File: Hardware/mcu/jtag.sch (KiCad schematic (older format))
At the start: 1 part, among them P301 ARM_JTAG_10PIN

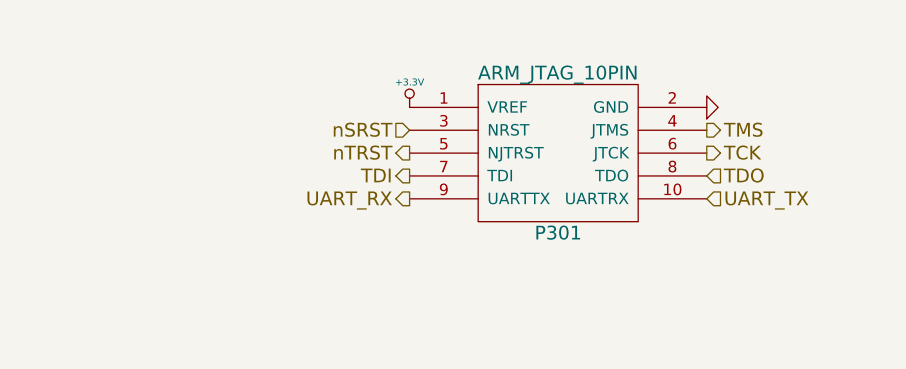
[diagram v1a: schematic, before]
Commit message: changes to mcu, new format and using a display adapter board
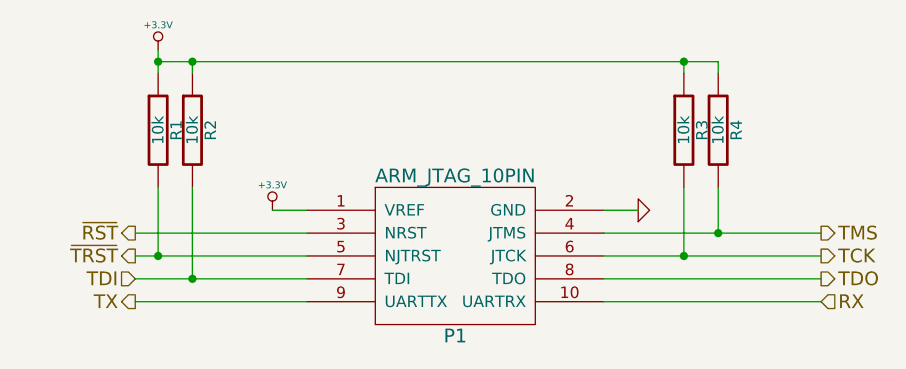
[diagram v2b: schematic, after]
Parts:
- removed P301: ARM_JTAG_10PIN, symbol ARM_JTAG_10PIN
- added P1: ARM_JTAG_10PIN, symbol ARM_JTAG_10PIN
- added R1, R2, R3, R4: 10k, symbol R
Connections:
- net +3.3V: now also P1.1 (VREF), R1.1, R2.1, R3.1, R4.1
- net GND: now also P1.2 (GND)
- net TCK: now also P1.6 (JTCK), R3.2
- net TDI: now also P1.7 (TDI), R2.2
- net TDO: now also P1.8 (TDO)
- net TMS: now also P1.4 (JTMS), R4.2
- new net RX: P1.10 (UARTRX)
- new net TX: P1.9 (UARTTX)
- new net ~RST: P1.3 (NRST)
- new net ~TRST: P1.5 (NJTRST), R1.2
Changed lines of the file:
@@
-EESchema Schematic File Version 2  date Di 17 Mai 2011 02:16:23 CEST
+EESchema Schematic File Version 2  date So 17 Jul 2011 02:24:16 CEST
 LIBS:power
 LIBS:device
@@
 LIBS:valves
 LIBS:nhesse
-LIBS:bordcomputer-cache
+LIBS:mcu-cache
 EELAYER 25  0
 EELAYER END
@@
 Sheet 3 9
 Title ""
-Date "17 may 2011"
+Date "16 jul 2011"
 Rev ""
 Comp ""
@@
 Comment4 ""
 $EndDescr
+Connection ~ 4850 2250
+Wire Wire Line
+	4850 2050 4850 2250
+Connection ~ 2550 1500
+Wire Wire Line
+	4700 1500 4700 1550
+Connection ~ 2550 2450
+Wire Wire Line
+	2550 2050 2550 2450
+Wire Wire Line
+	2400 1450 2400 1550
+Wire Wire Line
+	4350 2550 5300 2550
+Wire Wire Line
+	4350 2450 5300 2450
+Wire Wire Line
+	4350 2350 5300 2350
+Wire Wire Line
+	4350 2250 5300 2250
+Wire Wire Line
+	4500 2150 4350 2150
+Wire Wire Line
+	2900 2150 3050 2150
+Wire Wire Line
+	2300 2250 3050 2250
+Wire Wire Line
+	2300 2350 3050 2350
+Wire Wire Line
+	2300 2450 3050 2450
+Wire Wire Line
+	2300 2550 3050 2550
+Wire Wire Line
+	2400 2050 2400 2350
+Connection ~ 2400 2350
+Wire Wire Line
+	4700 2350 4700 2050
+Connection ~ 4700 2350
+Wire Wire Line
+	2550 1500 2550 1550
+Connection ~ 2400 1500
+Wire Wire Line
+	2400 1500 4850 1500
+Wire Wire Line
+	4850 1500 4850 1550
+Connection ~ 4700 1500
 $Comp
-L ARM_JTAG_10PIN P301
-U 1 1 4D77ED79
-P 4150 1900
-F 0 "P301" H 4150 1550 60  0000 C CNN
-F 1 "ARM_JTAG_10PIN" H 4150 2250 60  0000 C CNN
-	1    4150 1900
+L R R4
+U 1 1 4E175E60
+P 4850 1800
+F 0 "R4" V 4930 1800 50  0000 C CNN
+F 1 "10k" V 4850 1800 50  0000 C CNN
+	1    4850 1800
 	1    0    0    -1
 $EndComp
-Text HLabel 3500 1800 0    60   Input ~ 0
-nSRST
-Text HLabel 4800 2000 2    60   Input ~ 0
+$Comp
+L R R3
+U 1 1 4E1759C8
+P 4700 1800
+F 0 "R3" V 4780 1800 50  0000 C CNN
+F 1 "10k" V 4700 1800 50  0000 C CNN
+	1    4700 1800
+	1    0    0    -1
+$EndComp
+$Comp
+L R R2
+U 1 1 4E1759C4
+P 2550 1800
+F 0 "R2" V 2630 1800 50  0000 C CNN
+F 1 "10k" V 2550 1800 50  0000 C CNN
+	1    2550 1800
+	1    0    0    -1
+$EndComp
+$Comp
+L +3.3V #PWR06
+U 1 1 4E1759B0
+P 2400 1450
+F 0 "#PWR06" H 2400 1410 30  0001 C CNN
+F 1 "+3.3V" H 2400 1560 30  0000 C CNN
+	1    2400 1450
+	1    0    0    -1
+$EndComp
+$Comp
+L R R1
+U 1 1 4E17593B
+P 2400 1800
+F 0 "R1" V 2480 1800 50  0000 C CNN
+F 1 "10k" V 2400 1800 50  0000 C CNN
+	1    2400 1800
+	1    0    0    -1
+$EndComp
+Text HLabel 2300 2550 0    60   Output ~ 0
+TX
+Text HLabel 2300 2450 0    60   Input ~ 0
+TDI
+Text HLabel 2300 2350 0    60   Output ~ 0
+~TRST
+Text HLabel 2300 2250 0    60   Output ~ 0
+~RST
+Text HLabel 5300 2550 2    60   Input ~ 0
+RX
+Text HLabel 5300 2450 2    60   Output ~ 0
 TDO
-Text HLabel 4800 1900 2    60   Output ~ 0
+Text HLabel 5300 2350 2    60   Output ~ 0
 TCK
-Text HLabel 4800 1800 2    60   Output ~ 0
+Text HLabel 5300 2250 2    60   Output ~ 0
 TMS
-Text HLabel 3500 2000 0    60   Output ~ 0
-TDI
-Text HLabel 3500 1900 0    60   Output ~ 0
-nTRST
-Text HLabel 4800 2100 2    60   Input ~ 0
-UART_TX
-Text HLabel 3500 2100 0    60   Output ~ 0
-UART_RX
 $Comp
-L GND #PWR06
-U 1 1 4D3F5D14
-P 4800 1700
-F 0 "#PWR06" H 4800 1700 30  0001 C CNN
-F 1 "GND" H 4800 1630 30  0001 C CNN
-	1    4800 1700
+L GND #PWR07
+U 1 1 4E1758CF
+P 4500 2150
+F 0 "#PWR07" H 4500 2150 30  0001 C CNN
+F 1 "GND" H 4500 2080 30  0001 C CNN
+	1    4500 2150
 	0    -1   -1   0
 $EndComp
 $Comp
-L +3.3V #PWR07
-U 1 1 4D3F5D04
-P 3500 1700
-F 0 "#PWR07" H 3500 1660 30  0001 C CNN
-F 1 "+3.3V" H 3500 1810 30  0000 C CNN
-	1    3500 1700
+L +3.3V #PWR08
+U 1 1 4E1758CA
+P 2900 2150
+F 0 "#PWR08" H 2900 2110 30  0001 C CNN
+F 1 "+3.3V" H 2900 2260 30  0000 C CNN
+	1    2900 2150
 	1    0    0    -1
 $EndComp
+$Comp
+L ARM_JTAG_10PIN P1
+U 1 1 4E1758C3
+P 3700 2350
+F 0 "P1" H 3700 2000 60  0000 C CNN
+F 1 "ARM_JTAG_10PIN" H 3700 2700 60  0000 C CNN
+	1    3700 2350
+	1    0    0    -1
+$EndComp
